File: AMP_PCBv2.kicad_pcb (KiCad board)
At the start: 2 copper layers, 100.1 x 100.1 mm, 114 parts, among them J1 POWER, J2 EBRAKE, J3 MC, J4 STEERING, J5 OLED Breakout, J6 EBRAKE_BREAKOUT, Q1 Q_NMOS_GDS, Q2 Q_NMOS_GDS, Q3 Q_NMOS_GDS, Q4 Q_NMOS_GDS, U1 Teensy4.0, U10 RFM9x, U2 FT234XD, U3 LM1117-ADJ, U4 LM1117-ADJ, U5 74HC157, U6 74HC157, U7 74HC4060, U8 74HC00, U9 TLV272

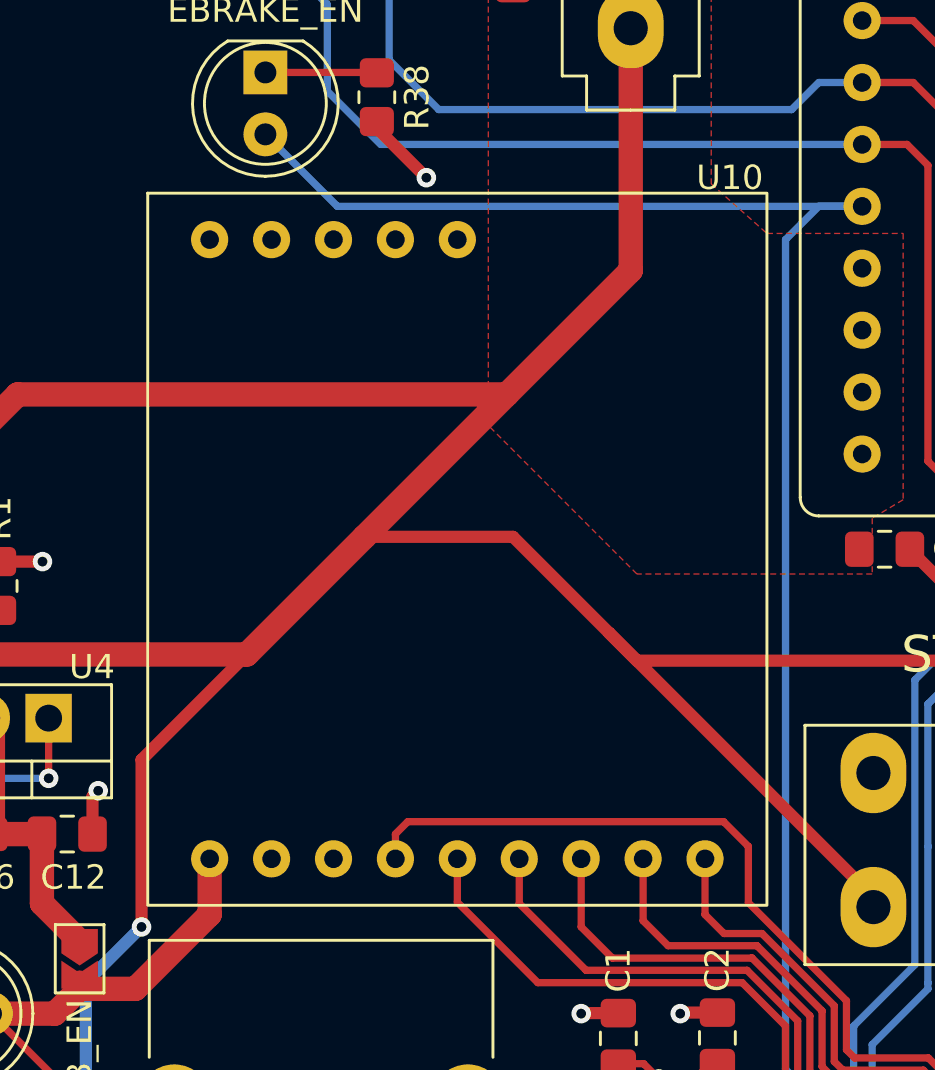
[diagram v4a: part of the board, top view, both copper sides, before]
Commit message: Add 3D models
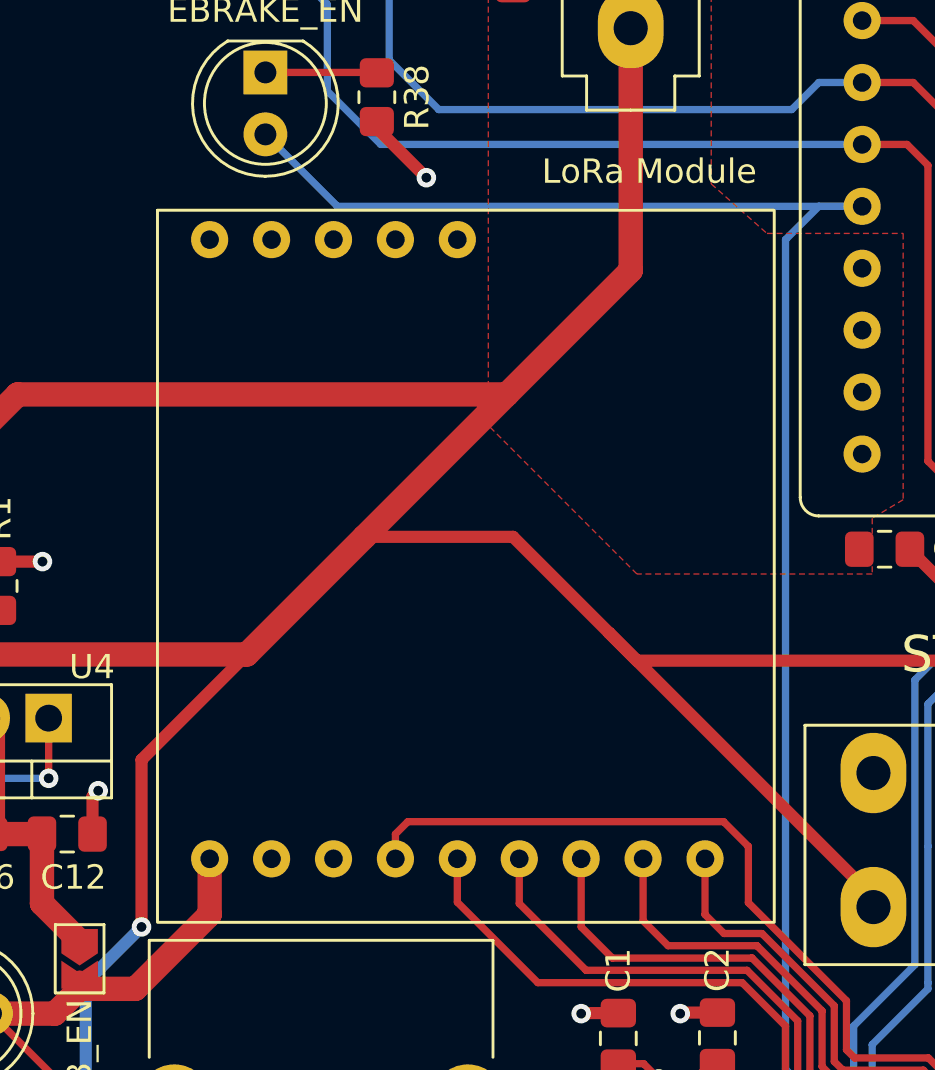
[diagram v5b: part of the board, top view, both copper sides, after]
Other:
- board text added: "LoRa Module"
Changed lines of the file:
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@@
     (pad "13" smd rect locked (at 0 0) (size 1.6 2.5) (layers "F.Cu" "F.Mask")
       (net 2 "GND") (pinfunction "GND") (pintype "power_in"))
-    (model "${KICAD6_3DMODEL_DIR}/Package_DFN_QFN.3dshapes/DFN-12-1EP_3x3mm_P0.5mm_EP1.6x2.5mm.wrl"
+    (model "${KICAD6_3DMODEL_DIR}/Package_DFN_QFN.3dshapes/DFN-12-1EP_3x3mm_P0.5mm_EP2.05x2.86mm.wrl"
       (offset (xyz 0 0 0))
       (scale (xyz 1 1 1))
@@
     (pad "26" thru_hole circle (at 2.54 2.54 90) (size 1.524 1.524) (drill 0.762) (layers *.Cu *.Mask)
       (net 9 "+12V") (pinfunction "Pin_26") (pintype "passive"))
+    (model "${KIPRJMOD}/libs/3Dmodels/Brake_Controller.step"
+      (offset (xyz 18.5 -18 2.5))
+      (scale (xyz 1 1 1))
+      (rotate (xyz 0 0 0))
+    )
   )
   (footprint "Connector_PinHeader_2.54mm:PinHeader_1x03_P2.54mm_Vertical" (layer "F.Cu")
@@
     (property "Sheetname" "")
     (attr through_hole)
-    (fp_text reference "U10" (at 21.336 -2.54 unlocked) (layer "F.SilkS")
+    (fp_text reference "U10" (at 21.336 -2.54 unlocked) (layer "F.SilkS") hide
       (effects (font (size 1 1) (thickness 0.15)))
     )
@@
       (effects (font (size 1 1) (thickness 0.15)))
     )
-    (fp_rect (start -2.54 -1.905) (end 22.86 27.305) (layer "F.SilkS") (width 0.12) (fill none))
+    (fp_rect (start -2.14 -1.205) (end 23.16 28.005) (layer "F.SilkS") (width 0.12) (fill none))
     (pad "1" thru_hole circle (at 0 25.4 90) (size 1.524 1.524) (drill 0.762) (layers *.Cu *.Mask)
       (net 4 "+3V3") (pinfunction "VIN") (pintype "power_in"))
@@
     (pad "14" thru_hole circle (at 10.16 0) (size 1.524 1.524) (drill 0.762) (layers *.Cu *.Mask)
       (net 127 "unconnected-(U10-Pad14)") (pinfunction "G5") (pintype "input"))
+    (model "${KIPRJMOD}/libs/3Dmodels/Adafruit_RFM9x.step"
+      (offset (xyz -2.5 -28 0))
+      (scale (xyz 1 1 1))
+      (rotate (xyz -90 0 0))
+    )
   )
   (footprint "Connector_PinHeader_2.54mm:PinHeader_1x14_P2.54mm_Vertical" (layer "F.Cu")
@@
     (pad "2" thru_hole oval (at 0 5.5) (size 2.7 3.3) (drill 1.4) (layers *.Cu *.Mask)
       (net 45 "/OUT_EBRAKE1") (pinfunction "Pin_2") (pintype "passive"))
-    (model "${KICAD6_3DMODEL_DIR}/Connector_Molex.3dshapes/Molex_Mini-Fit_Jr_5566-02A_2x01_P4.20mm_Vertical.wrl"
-      (offset (xyz 0 0 0))
+    (model "${KIPRJMOD}/libs/3Dmodels/Molex_Mini-Fit-Jr_5566_2pos.stp"
+      (offset (xyz 0 -2.5 0))
       (scale (xyz 1 1 1))
-      (rotate (xyz 0 0 0))
+      (rotate (xyz -90 0 180))
     )
   )
@@
     (pad "8" thru_hole oval (at 12.6 5.5 180) (size 2.7 3.3) (drill 1.4) (layers *.Cu *.Mask)
       (net 2 "GND") (pinfunction "Pin_8") (pintype "passive"))
-    (model "${KICAD6_3DMODEL_DIR}/Connector_Molex.3dshapes/Molex_Mini-Fit_Jr_5566-08A_2x04_P4.20mm_Vertical.wrl"
-      (offset (xyz 0 0 0))
+    (model "${KIPRJMOD}/libs/3Dmodels/Molex_Mini-Fit-Jr_5566_8pos.stp"
+      (offset (xyz 6 -2.5 0))
       (scale (xyz 1 1 1))
-      (rotate (xyz 0 0 0))
+      (rotate (xyz -90 0 180))
     )
   )
@@
     (pad "2" thru_hole oval (at 0 5.5) (size 2.7 3.3) (drill 1.4) (layers *.Cu *.Mask)
       (net 9 "+12V") (pinfunction "Pin_2") (pintype "passive"))
-    (model "${KICAD6_3DMODEL_DIR}/Connector_Molex.3dshapes/Molex_Mini-Fit_Jr_5566-02A_2x01_P4.20mm_Vertical.wrl"
-      (offset (xyz 0 0 0))
+    (model "${KIPRJMOD}/libs/3Dmodels/Molex_Mini-Fit-Jr_5566_2pos.stp"
+      (offset (xyz 0 -2.5 0))
       (scale (xyz 1 1 1))
-      (rotate (xyz 0 0 0))
+      (rotate (xyz -90 0 180))
     )
   )
@@
     (pad "8" thru_hole oval (at 12.6 5.5 180) (size 2.7 3.3) (drill 1.4) (layers *.Cu *.Mask)
       (net 48 "unconnected-(J3-Pad8)") (pinfunction "Pin_8") (pintype "passive+no_connect"))
-    (model "${KICAD6_3DMODEL_DIR}/Connector_Molex.3dshapes/Molex_Mini-Fit_Jr_5566-08A_2x04_P4.20mm_Vertical.wrl"
-      (offset (xyz 0 0 0))
+    (model "${KIPRJMOD}/libs/3Dmodels/Molex_Mini-Fit-Jr_5566_8pos.stp"
+      (offset (xyz 6 -2.5 0))
       (scale (xyz 1 1 1))
-      (rotate (xyz 0 0 0))
+      (rotate (xyz -90 0 180))
     )
   )
@@
     (pad "5" thru_hole circle (at -7.27 2.71 180) (size 3 3) (drill 2.3) (layers *.Cu *.Mask)
       (net 2 "GND") (pinfunction "Shield") (pintype "passive"))
-    (model "${KICAD6_3DMODEL_DIR}/Connector_USB.3dshapes/USB_B_TE_5787834_Vertical.wrl"
-      (offset (xyz 0 0 0))
+    (model "${KIPRJMOD}/libs/3Dmodels/CUI_DEVICES_UJ2-BV-1-TH.step"
+      (offset (xyz -1 -6.5 15.5))
       (scale (xyz 1 1 1))
       (rotate (xyz 0 0 0))
@@
     (effects (font (size 1 1) (thickness 0.15)))
   )
+  (gr_text "LoRa Module" (at 122.428 71.12) (layer "F.SilkS")
+    (effects (font (size 1 1) (thickness 0.2)))
+  )
   (gr_text "12V" (at 121.666 55.88) (layer "F.SilkS")
